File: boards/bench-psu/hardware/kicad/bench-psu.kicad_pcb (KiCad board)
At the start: 4 copper layers, 90 x 76 mm, 87 parts, among them J1 TYPE-C 16PIN 2MD(073), J2 DG301-5.0-04P-14-1000A(H), J3 PZ254V-11-04P, J4 PZ254V-11-05P, Q1 AO4407A, SW1 TS-1187A-B-A-B, SW2 TS-1187A-B-A-B, U1 STUSB4500QTR, U11 LMR51635YDDCR, U12 INA219AIDCNR, U2 USBLC6-2SC6, U21 LMR51635YDDCR, U22 INA219AIDCNR, U3 LMR51635YDDCR, U4 AP2112K-3.3TRG1, U5 ESP32-S3-MINI-1-N8

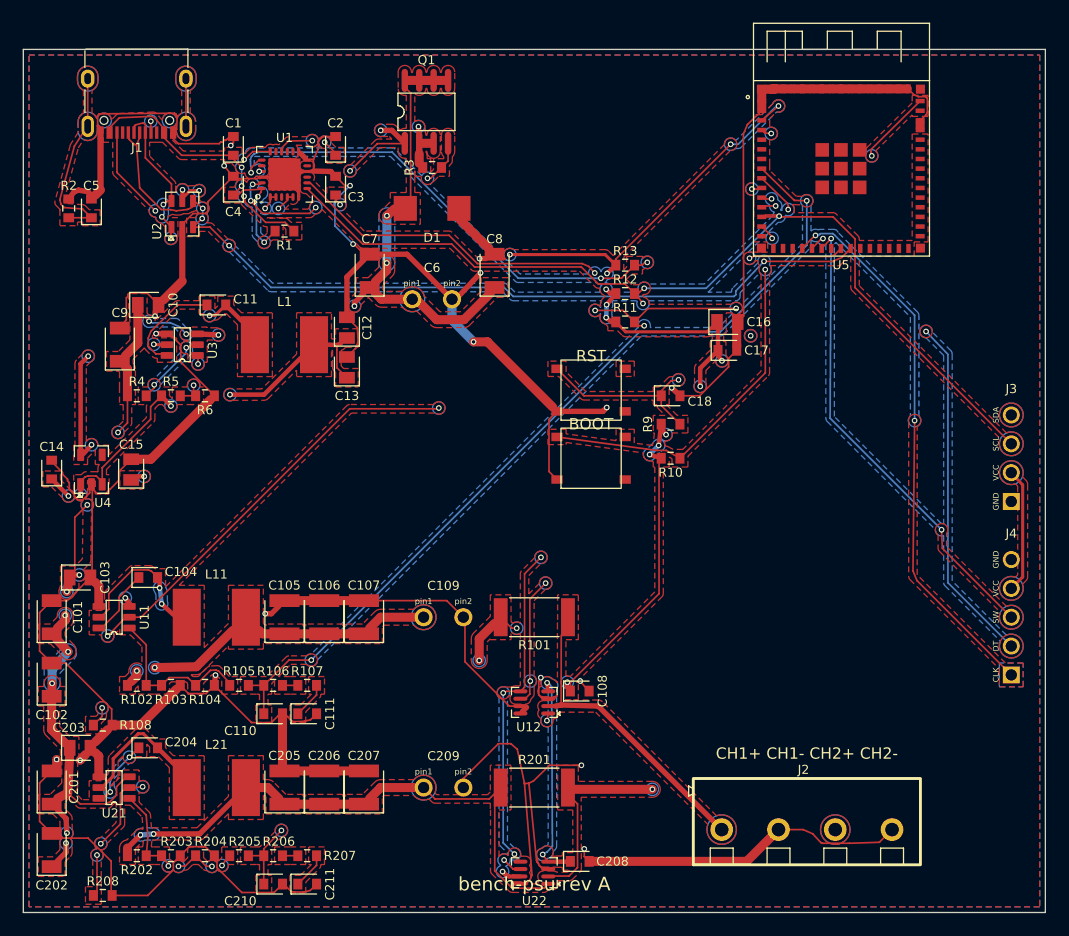
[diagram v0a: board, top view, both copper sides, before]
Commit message: bench-psu rev B: LMR33630 bucks, INA226 with hardware over-current trip, fail-safe FB current sink
- Converter: LMR33630A (400 kHz, 3 A) per channel and for the 5 V rail; FXL1040 10 uH inductor
- Voltage set: TLV9062 + NPN current sink on FB (1.6 V at 0 V/floating PWM, 16.6 V max)
- Loop compensation: 6.8k + 220 nF lag network on FB (simulated PM 52-75 deg)
- Measurement: INA226 on 20 mR shunt; ALERT pulls buck EN low (hardware trip)
- Input: SMBJ22A TVS, gate divider for AO4407A Vgs, SMD electrolytic
- Add SPICE sim decks, scripts, plots (boards/bench-psu/sim)
- Regenerate review set and fab files; update README

Co-Authored-By: Claude Opus 5.5 <noreply@anthropic.com>
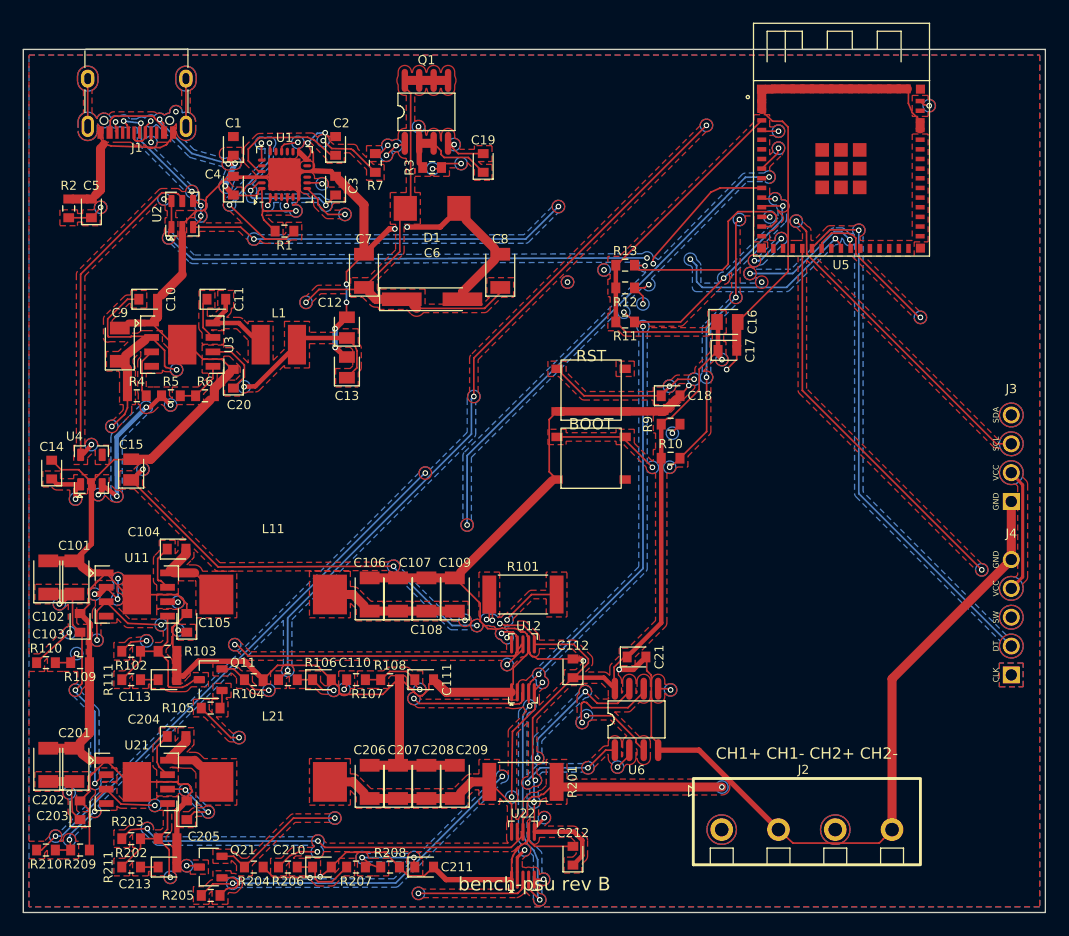
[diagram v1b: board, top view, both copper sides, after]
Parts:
- added C112: 100nF, tscircuit:capacitor_cap0603, F.Cu at (103.4, 116.5)
- added C113: 220nF, tscircuit:capacitor_cap0603, F.Cu at (67.7, 117.5)
- added C19: 100nF, tscircuit:capacitor_cap0603, F.Cu at (95.5, 72.0)
- added C20: 1uF, tscircuit:capacitor_cap0603, F.Cu at (73.5, 91.0)
- added C21: 100nF, tscircuit:capacitor_cap0603, F.Cu at (109.0, 115.5)
- added C212: 100nF, tscircuit:capacitor_cap0603, F.Cu at (103.4, 133.0)
- added C213: 220nF, tscircuit:capacitor_cap0603, F.Cu at (67.7, 134.0)
- added Q11: MMBT3904(RANGE:100-300), tscircuit:MMBT3904_RANGE_100-300, F.Cu at (71.5, 117.5)
- added Q21: MMBT3904(RANGE:100-300), tscircuit:MMBT3904_RANGE_100-300, F.Cu at (71.5, 134.0)
- added R109: 100kΩ, tscircuit:resistor_res0603, F.Cu at (60.0, 116.0)
- added R110: 10kΩ, tscircuit:resistor_res0603, F.Cu at (57.0, 116.0)
- added R111: 6.8kΩ, tscircuit:resistor_res0603, F.Cu at (64.5, 117.5)
- added R209: 100kΩ, tscircuit:resistor_res0603, F.Cu at (60.0, 132.5)
- added R210: 10kΩ, tscircuit:resistor_res0603, F.Cu at (57.0, 132.5)
- added R211: 6.8kΩ, tscircuit:resistor_res0603, F.Cu at (64.5, 134.0)
- added R7: 47kΩ, tscircuit:resistor_res0603, F.Cu at (86.0, 72.0)
- added U6: TLV9062IDR, tscircuit:TLV9062IDR, F.Cu at (109.0, 121.0)
- C10, C103, C203: footprint tscircuit:capacitor_cap0805 -> tscircuit:capacitor_cap0603
- C101, C102, C201, C202, C7, C8, C9: value 2.2uF -> 10uF
- C105, C205: value 4.7uF -> 1uF; footprint tscircuit:capacitor_cap1210 -> tscircuit:capacitor_cap0603
- C106, C107, C206, C207: value 4.7uF -> 22uF; footprint tscircuit:capacitor_cap1210 -> tscircuit:capacitor_cap1206
- C108, C208: value 100nF -> 22uF; footprint tscircuit:capacitor_cap0603 -> tscircuit:capacitor_cap1206
- C109, C209: value 100uF -> 22uF; footprint tscircuit:NXA63V100M8_15_LO -> tscircuit:capacitor_cap1206
- C6: footprint tscircuit:NXA63V100M8_15_LO -> tscircuit:RVT1V101M0607_100UF_35V
- D1: value SMBJ24A -> SMBJ22A; footprint tscircuit:SMBJ24A -> tscircuit:SMBJ22A
- L1: value 10µH -> 15µH; footprint tscircuit:SWPA6045S100MT -> tscircuit:SWPA4030S150MT
- L11, L21: footprint tscircuit:SWPA6045S100MT -> tscircuit:FXL1040-100-M
- R101, R201: value 100mΩ -> 20mΩ
- R102, R202: value 100kΩ -> 120kΩ
- R103, R203: value 12kΩ -> 200kΩ
- R104, R204: value 12kΩ -> 2.4kΩ
- R105, R205: value 20kΩ -> 1kΩ
- R107, R207: value 10kΩ -> 100kΩ
- R108, R208: value 100kΩ -> 10kΩ
- R6: value 20kΩ -> 24kΩ
- U11, U21, U3: value LMR51635YDDCR -> LMR33630ADDAR; footprint tscircuit:LMR51635YDDCR -> tscircuit:LMR33630ADDAR
- U12, U22: value INA219AIDCNR -> INA226AIDGSR; footprint tscircuit:INA219AIDCNR -> tscircuit:INA226AIDGSR
- moved R108 25.6 mm to (87.3, 117.5)
- moved R208 25.4 mm to (87.3, 134.0)
- moved C108 16.0 mm to (90.5, 110.0), turned to 90 degrees
- moved C208 15.2 mm to (90.5, 126.5), turned to 90 degrees
- moved C111 10.7 mm to (90.3, 117.5)
- moved C211 10.4 mm to (90.3, 134.0)
- moved C102 9.00 mm to (57.2, 108.5)
- moved C205 8.83 mm to (69.4, 129.0)
- moved C105 8.61 mm to (69.4, 112.5)
- moved C202 7.51 mm to (57.2, 125.0)
- moved C203 5.50 mm to (60.0, 129.0), turned to 90 degrees
- moved L11 5.39 mm to (77.0, 110.0)
- moved C110 5.24 mm to (81.3, 117.5)
- moved L21 5.02 mm to (77.0, 126.5)
- moved C210 4.55 mm to (81.3, 134.0)
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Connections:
- C104 pad 1: U11_CB -> U11_BOOT
- C104 pad 2: SW1 -> SW_CH1
- C105 pad 1: OUT1_B -> U11_VCC
- C108 pad 1: V3V3 -> OUT1_B
- C11 pad 1: U3_CB -> U3_BOOT
- C110 pad 1: PWM1 -> PWM1_F
- C111 pad 1: Net-(R107-Pad2) -> VSET1
- C204 pad 1: U21_CB -> U21_BOOT
- C204 pad 2: SW2 -> SW_CH2
- C205 pad 1: OUT2_B -> U21_VCC
- C208 pad 1: V3V3 -> OUT2_B
- C210 pad 1: PWM2 -> PWM2_F
- C211 pad 1: Net-(R207-Pad2) -> VSET2
- L11 pad 1: SW1 -> SW_CH1
- L21 pad 1: SW2 -> SW_CH2
- R102 pad 1: OUT1_B -> OUT1
- R104 pad 1: FB1 -> ISET1_E
- R105 pad 1: FB1 -> ISET1_DRV
- R105 pad 2: PWM1 -> Q11_B
- R106 pad 2: Net-(R106-Pad2) -> PWM1_F
- R107 pad 1: Net-(R106-Pad2) -> PWM1_F
- R107 pad 2: Net-(R107-Pad2) -> VSET1
- R108 pad 1: EN1 -> VSET1
- R202 pad 1: OUT2_B -> OUT2
- R204 pad 1: FB2 -> ISET2_E
- R205 pad 1: FB2 -> ISET2_DRV
- R205 pad 2: PWM2 -> Q21_B
- R206 pad 2: Net-(R206-Pad2) -> PWM2_F
- R207 pad 1: Net-(R206-Pad2) -> PWM2_F
- R207 pad 2: Net-(R207-Pad2) -> VSET2
- R208 pad 1: EN2 -> VSET2
- U1 pad 16: PD_GATE -> PD_EN
- U11 pad 1: FB1 -> GND
- U11 pad 2: EN1 -> VIN
- U11 pad 3: VIN -> EN1
- U11 pad 4: GND -> (no net)
- U11 pad 5: SW1 -> FB1
- U11 pad 6: U11_CB -> U11_VCC
- U12 pad 1: OUT1_B -> GND
- U12 pad 2: OUT1 -> GND
- U12 pad 3: GND -> EN1
- U12 pad 4: V3V3 -> I2C_SDA
- U12 pad 6: I2C_SDA -> V3V3
- U12 pad 8: GND -> OUT1
- U21 pad 1: FB2 -> GND
- U21 pad 2: EN2 -> VIN
- U21 pad 3: VIN -> EN2
- U21 pad 4: GND -> (no net)
- U21 pad 5: SW2 -> FB2
- U21 pad 6: U21_CB -> U21_VCC
- U22 pad 1: OUT2_B -> GND
- U22 pad 2: OUT2 -> V3V3
- U22 pad 3: GND -> EN2
- U22 pad 4: V3V3 -> I2C_SDA
- U22 pad 6: I2C_SDA -> V3V3
- U22 pad 7: V3V3 -> GND
- U22 pad 8: GND -> OUT2
- U3 pad 1: FB5 -> GND
- U3 pad 2: U3_EN -> VIN
- U3 pad 3: VIN -> U3_EN
- U3 pad 4: GND -> (no net)
- U3 pad 5: SW5 -> FB5
- U3 pad 6: U3_CB -> U3_VCC
- U5 pad 10: EN1 -> EN1_MCU
- U5 pad 11: EN2 -> EN2_MCU
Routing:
- net EN2_MCU: track 0.00 -> 92.7 mm, vias 0 -> 4
- net EN1_MCU: track 0.00 -> 80.7 mm, vias 0 -> 4
- net GND: track 440.1 -> 380.9 mm, vias 19 -> 14
- net EN2: track 102.0 -> 47.4 mm
- net ISET2_DRV: track 0.00 -> 46.6 mm, vias 0 -> 4
- net OUT1: track 25.3 -> 70.0 mm, vias 0 -> 5
- net ISET2_E: track 0.00 -> 43.8 mm, vias 0 -> 2
- net ISET1_DRV: track 0.00 -> 39.8 mm, vias 0 -> 3
- net ISET1_E: track 0.00 -> 38.2 mm, vias 0 -> 2
- net VSET2: track 0.00 -> 36.3 mm, vias 0 -> 3
- net OUT2: track 32.9 -> 67.0 mm, vias 1 -> 3
- net EN1: track 80.7 -> 47.9 mm
- net OUT1_B: track 40.4 -> 11.3 mm, vias 5 -> 4
- net OUT2_B: track 38.6 -> 11.0 mm, vias 2 -> 0
- net VSET1: track 0.00 -> 25.9 mm, vias 0 -> 2
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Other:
- board text added: "bench-psu rev B"
- board text removed: "bench-psu rev A"

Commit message: bench-psu: output status LEDs, silkscreen pass, bring-up guide
- Per channel ON LED (KT-0603YG, driven from the buck EN node through an NPN: shows the
  hardware state, dark after an INA226 trip) and OC LED (KT-0603R on IO21 / IO47)
- Silkscreen: LED functions, header pin labels at fab-legal size, RST/BOOT and the title
  moved off parts and pads, rail probe points (VIN, 5V, 3V3), PD input label, pin and
  I2C-address summary on the back
- README: bring-up guide (unpowered checks, logic at 5 V, firmware/I2C, channels at 5 V,
  20 V), LED design notes, pin map
- Republished review set; findings.toml from the new check verification

hardware/fab (gerbers, CPL) is NOT regenerated and still shows the board without LEDs:
`pcb fab` now needs `check --strict`, which fails on the open verification items.

Co-Authored-By: Claude Opus 5.5 <noreply@anthropic.com>
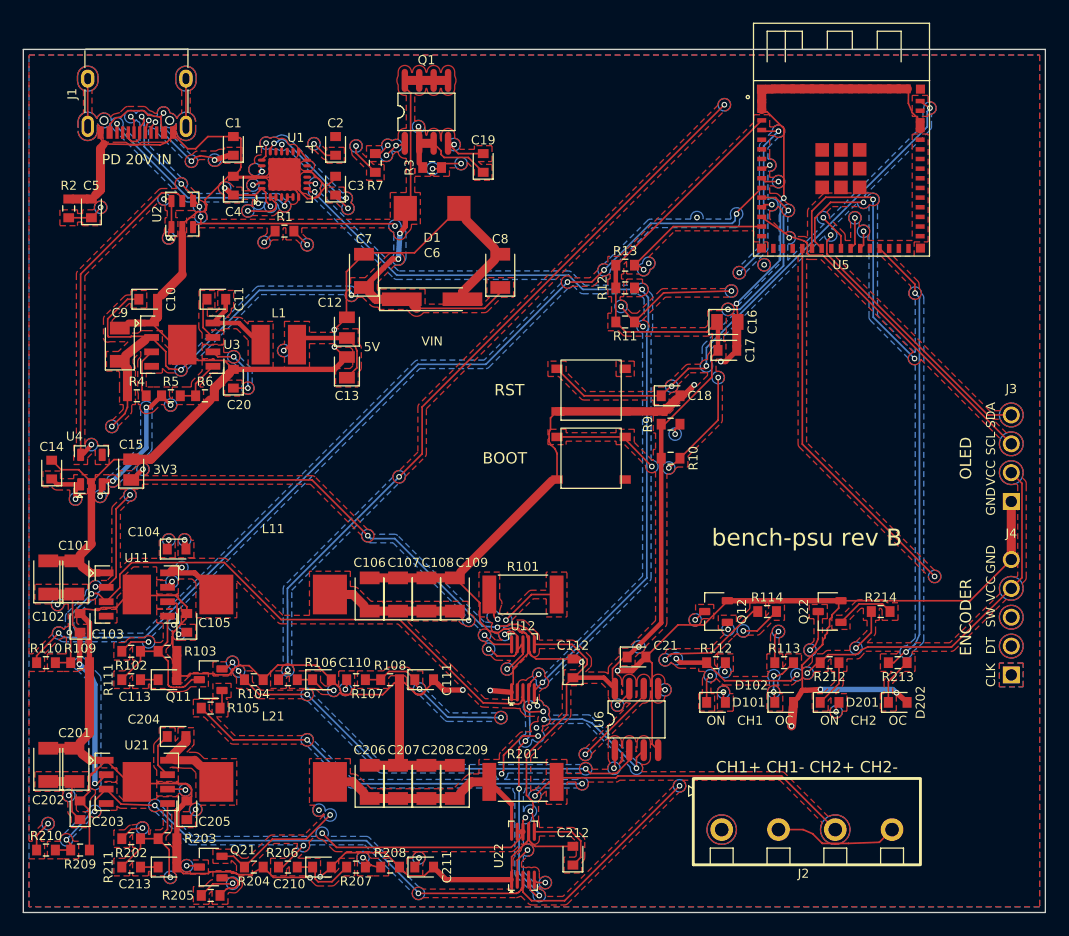
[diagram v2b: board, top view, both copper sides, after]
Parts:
- added D101: KT-0603YG, tscircuit:KT-0603YG, F.Cu at (116.0, 119.5)
- added D102: KT-0603R, tscircuit:KT-0603R, F.Cu at (122.0, 119.5)
- added D201: KT-0603YG, tscircuit:KT-0603YG, F.Cu at (126.0, 119.5)
- added D202: KT-0603R, tscircuit:KT-0603R, F.Cu at (132.0, 119.5)
- added Q12: MMBT3904(RANGE:100-300), tscircuit:MMBT3904_RANGE_100-300, F.Cu at (116.0, 111.5)
- added Q22: MMBT3904(RANGE:100-300), tscircuit:MMBT3904_RANGE_100-300, F.Cu at (126.0, 111.5)
- added R112: 1kΩ, tscircuit:resistor_res0603, F.Cu at (116.0, 116.0)
- added R113: 1kΩ, tscircuit:resistor_res0603, F.Cu at (122.0, 116.0)
- added R114: 47kΩ, tscircuit:resistor_res0603, F.Cu at (120.5, 111.5)
- added R212: 1kΩ, tscircuit:resistor_res0603, F.Cu at (126.0, 116.0)
- added R213: 1kΩ, tscircuit:resistor_res0603, F.Cu at (132.0, 116.0)
- added R214: 47kΩ, tscircuit:resistor_res0603, F.Cu at (130.5, 111.5)
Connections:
- U5 pad 25: (no net) -> LED_OC1
- U5 pad 27: (no net) -> LED_OC2
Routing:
- net EN2: track 47.4 -> 89.7 mm, vias 4 -> 6
- net LED_OC1: track 0.00 -> 42.3 mm, vias 0 -> 2
- net LED_OC2: track 0.00 -> 38.8 mm, vias 0 -> 2
- net GND: track 380.9 -> 415.6 mm, vias 14 -> 15
- net EN1: track 47.9 -> 77.0 mm
- net Q22_C: track 0.00 -> 10.3 mm, vias 0 -> 2
- net Q12_C: track 0.00 -> 8.62 mm, vias 0 -> 2
- net ENC_SW: track 42.7 -> 49.5 mm
- net ENC_B: track 46.6 -> 53.3 mm, vias 1 -> 2
- net PD_ALERT: track 58.7 -> 52.1 mm
- net V3V3: track 215.0 -> 219.9 mm
- net PWM2: track 81.2 -> 86.0 mm
- net Q12_B: track 0.00 -> 4.67 mm, vias 0 -> 2
- net Q22_B: track 0.00 -> 4.45 mm
- net VBUS: track 48.1 -> 52.2 mm, vias 8 -> 10
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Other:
- board text added: "3V3"
- board text added: "5V"
- board text added: "CH1"
- board text added: "CH1 / CH2: 1.6-16.6 V, 3 A, hardware OC trip"
- board text added: "CH2"
- board text added: "CLK"
- board text added: "DT"
- board text added: "ENCODER"
- board text added: "GND"
- board text added: "I2C IO8/IO9: INA226 0x40 / 0x41, STUSB4500 0x28, OLED 0x3C"
- board text added: "OC"
- board text added: "OLED"
- board text added: "ON"
- board text added: "PD 20V IN"
- board text added: "PWM IO4/IO5 EN IO6/IO7 OC LED IO21/IO47 ENC IO15/16/17"
- board text added: "SCL"
- board text added: "SDA"
- board text added: "SW"
- board text added: "VCC"
- board text added: "VIN"
- board text added: "bench-psu rev B - USB-C PD 20 V in"
